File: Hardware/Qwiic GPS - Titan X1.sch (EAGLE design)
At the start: 33 parts, among them J1 U.FL, J2 SMD, J3 PTH, J4 SMD, U1 TITAN X1 GPS

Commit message: Added SparkX models to Sparkfun Library
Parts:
- B1: value COIN CELL -> 6.8MM_COIN_CELL; device SparkX:6.8MM_COIN_CELL -> SparkFun-Batteries:BATTERY-6.8MM_SMD
- J1: device SparkX:U.FL -> SparkFun-Connectors:U.FL2PIN
- J2, J4: value SMD -> Qwiic Right Angle; device SparkX:I2C_STANDARDJS-1MM -> SparkFun-Connectors:I2C_STANDARDQWIIC
- U1: value TITAN X1 GPS -> Titan X1 GPS; device SparkX:TITAN_X1_GPS -> SparkFun-GPS:TITAN_X1_GPS
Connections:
- net 3.3V: now also J2.2, J4.2; no longer J2.VCC, J4.VCC
- net GND: now also J2.1, J4.1; no longer J2.GND, J4.GND
- net SCL: now also J2.4, J4.4; no longer J2.SCL, J4.SCL
- net SDA: now also J2.3, J4.3; no longer J2.SDA, J4.SDA
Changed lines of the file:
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@@
 <part name="JP6" library="SparkFun" deviceset="FIDUCIAL" device="UFIDUCIAL"/>
 <part name="SUPPLY4" library="SparkFun-PowerSymbols" deviceset="3.3V" device=""/>
-<part name="J2" library="SparkX" deviceset="I2C_STANDARD" device="JS-1MM" value="SMD"/>
+<part name="J2" library="SparkFun-Connectors" deviceset="I2C_STANDARD" device="QWIIC" value="Qwiic Right Angle"/>
 <part name="GND6" library="SparkFun" deviceset="GND" device=""/>
 <part name="SUPPLY7" library="SparkFun-PowerSymbols" deviceset="3.3V" device=""/>
@@
 <part name="FRAME1" library="SparkFun-Aesthetics" deviceset="FRAME-LETTER" device=""/>
 <part name="SUPPLY8" library="SparkFun-PowerSymbols" deviceset="3.3V" device=""/>
-<part name="J4" library="SparkX" deviceset="I2C_STANDARD" device="JS-1MM" value="SMD"/>
+<part name="J4" library="SparkFun-Connectors" deviceset="I2C_STANDARD" device="QWIIC" value="Qwiic Right Angle"/>
 <part name="GND8" library="SparkFun" deviceset="GND" device=""/>
 <part name="LOGO1" library="SparkFun-Aesthetics" deviceset="OSHW-LOGO" device="MINI"/>
@@
 <part name="FB1" library="SparkFun-Coils" deviceset="FERRITE_BEAD" device="-0603" value="600Ohm/100MHz"/>
 <part name="C3" library="SparkFun-Capacitors" deviceset="1.0UF" device="-0603-16V-10%" value="1.0uF"/>
-<part name="B1" library="SparkX" deviceset="6.8MM_COIN_CELL" device="" value="COIN CELL"/>
+<part name="B1" library="SparkFun-Batteries" deviceset="BATTERY" device="-6.8MM_SMD" value="6.8MM_COIN_CELL"/>
 <part name="GND5" library="SparkFun-PowerSymbols" deviceset="GND" device=""/>
 <part name="GND9" library="SparkFun-PowerSymbols" deviceset="GND" device=""/>
 <part name="GND10" library="SparkFun-PowerSymbols" deviceset="GND" device=""/>
 <part name="GND11" library="SparkFun-PowerSymbols" deviceset="GND" device=""/>
-<part name="U1" library="SparkX" deviceset="TITAN_X1_GPS" device="" value="TITAN X1 GPS"/>
+<part name="U1" library="SparkFun-GPS" deviceset="TITAN_X1_GPS" device="" value="Titan X1 GPS"/>
 <part name="SUPPLY6" library="SparkFun-PowerSymbols" deviceset="3.3V" device=""/>
 <part name="R7" library="SparkFun-Resistors" deviceset="4.7KOHM" device="-0603-1/10W-1%" value="4.7k"/>
@@
 <part name="J7" library="SparkFun-Connectors" deviceset="CONN_05" device="NO_SILK"/>
 <part name="R11" library="SparkFun-Resistors" deviceset="470OHM" device="-0603-1/10W-1%" value="470"/>
-<part name="J1" library="SparkX" deviceset="U.FL" device="" value="U.FL"/>
+<part name="J1" library="SparkFun-Connectors" deviceset="U.FL2PIN" device="" value="U.FL"/>
 <part name="LOGO2" library="SparkFun-Aesthetics" deviceset="SFE_LOGO_NAME_FLAME" device=".1_INCH"/>
 </parts>
@@
 <instance part="JP6" gate="G$1" x="236.22" y="30.48"/>
 <instance part="SUPPLY4" gate="G$1" x="93.98" y="68.58"/>
-<instance part="J2" gate="G$1" x="104.14" y="60.96" rot="MR0"/>
+<instance part="J2" gate="G$1" x="104.14" y="60.96" smashed="yes" rot="MR0">
+<attribute name="VALUE" x="112.014" y="76.2" size="1.778" layer="96" font="vector" rot="MR270" align="top-left"/>
+<attribute name="NAME" x="109.22" y="68.834" size="1.778" layer="95" font="vector" rot="MR0"/>
+</instance>
 <instance part="GND6" gate="1" x="93.98" y="53.34"/>
 <instance part="SUPPLY7" gate="G$1" x="127" y="68.58"/>
@@
 <instance part="FRAME1" gate="V" x="147.32" y="0"/>
 <instance part="SUPPLY8" gate="G$1" x="93.98" y="40.64"/>
-<instance part="J4" gate="G$1" x="104.14" y="33.02" rot="MR0"/>
+<instance part="J4" gate="G$1" x="104.14" y="33.02" smashed="yes" rot="MR0">
+<attribute name="VALUE" x="112.014" y="48.26" size="1.778" layer="96" font="vector" rot="MR270" align="top-left"/>
+<attribute name="NAME" x="109.22" y="40.894" size="1.778" layer="95" font="vector" rot="MR0"/>
+</instance>
 <instance part="GND8" gate="1" x="93.98" y="25.4"/>
 <instance part="LOGO1" gate="G$1" x="233.68" y="48.26"/>
@@
 <net name="3.3V" class="0">
 <segment>
-<pinref part="J2" gate="G$1" pin="VCC"/>
+<pinref part="J2" gate="G$1" pin="2"/>
 <wire x1="96.52" y1="60.96" x2="93.98" y2="60.96" width="0.1524" layer="91"/>
 <wire x1="93.98" y1="60.96" x2="93.98" y2="68.58" width="0.1524" layer="91"/>
@@
 </segment>
 <segment>
-<pinref part="J4" gate="G$1" pin="VCC"/>
+<pinref part="J4" gate="G$1" pin="2"/>
 <wire x1="96.52" y1="33.02" x2="93.98" y2="33.02" width="0.1524" layer="91"/>
 <wire x1="93.98" y1="33.02" x2="93.98" y2="40.64" width="0.1524" layer="91"/>
@@
 <net name="GND" class="0">
 <segment>
-<pinref part="J2" gate="G$1" pin="GND"/>
+<pinref part="J2" gate="G$1" pin="1"/>
 <wire x1="96.52" y1="58.42" x2="93.98" y2="58.42" width="0.1524" layer="91"/>
 <wire x1="93.98" y1="58.42" x2="93.98" y2="55.88" width="0.1524" layer="91"/>
@@
 </segment>
 <segment>
-<pinref part="J4" gate="G$1" pin="GND"/>
+<pinref part="J4" gate="G$1" pin="1"/>
 <wire x1="96.52" y1="30.48" x2="93.98" y2="30.48" width="0.1524" layer="91"/>
 <wire x1="93.98" y1="30.48" x2="93.98" y2="27.94" width="0.1524" layer="91"/>
@@
 <net name="SCL" class="0">
 <segment>
-<pinref part="J2" gate="G$1" pin="SCL"/>
+<pinref part="J2" gate="G$1" pin="4"/>
 <wire x1="96.52" y1="66.04" x2="91.44" y2="66.04" width="0.1524" layer="91"/>
 <label x="91.44" y="66.04" size="1.27" layer="95" rot="R180" xref="yes"/>
@@
 </segment>
 <segment>
-<pinref part="J4" gate="G$1" pin="SCL"/>
+<pinref part="J4" gate="G$1" pin="4"/>
 <wire x1="96.52" y1="38.1" x2="91.44" y2="38.1" width="0.1524" layer="91"/>
 <label x="91.44" y="38.1" size="1.27" layer="95" rot="R180" xref="yes"/>
@@
 <net name="SDA" class="0">
 <segment>
-<pinref part="J2" gate="G$1" pin="SDA"/>
+<pinref part="J2" gate="G$1" pin="3"/>
 <wire x1="96.52" y1="63.5" x2="91.44" y2="63.5" width="0.1524" layer="91"/>
 <label x="91.44" y="63.5" size="1.27" layer="95" rot="R180" xref="yes"/>
@@
 </segment>
 <segment>
-<pinref part="J4" gate="G$1" pin="SDA"/>
+<pinref part="J4" gate="G$1" pin="3"/>
 <wire x1="96.52" y1="35.56" x2="91.44" y2="35.56" width="0.1524" layer="91"/>
 <label x="91.44" y="35.56" size="1.27" layer="95" rot="R180" xref="yes"/>

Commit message: fixed DRC errors, updated board to meet checklist
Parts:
- added JP7, JP8: FIDUCIALUFIDUCIAL, SparkFun:FIDUCIALUFIDUCIAL
- added LOGO3: REVISION, SparkFun-Aesthetics:REVISION
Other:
- note added: "Andrew England"
- note added: "V01"
- note removed: "X10"
- moved on the sheet: D1, JP5, R11
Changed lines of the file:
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@@
 <part name="J1" library="SparkFun-Connectors" deviceset="U.FL2PIN" device="" value="U.FL"/>
 <part name="LOGO2" library="SparkFun-Aesthetics" deviceset="SFE_LOGO_NAME_FLAME" device=".1_INCH"/>
+<part name="LOGO3" library="SparkFun-Aesthetics" deviceset="REVISION" device=""/>
+<part name="JP7" library="SparkFun" deviceset="FIDUCIAL" device="UFIDUCIAL"/>
+<part name="JP8" library="SparkFun" deviceset="FIDUCIAL" device="UFIDUCIAL"/>
 </parts>
 <sheets>
@@
 <plain>
 <text x="170.434" y="11.43" size="2.54" layer="94">N. Seidle</text>
-<text x="237.744" y="7.366" size="2.54" layer="94">X10</text>
+<text x="237.744" y="7.366" size="2.54" layer="94">V01</text>
 <text x="152.4" y="88.9" size="1.778" layer="97" align="center">7-bit unshifted I2C address: 0x10</text>
 <text x="153.162" y="165.862" size="2.54" layer="94" ratio="15" rot="MR180" align="center">Titan X1 GPS</text>
 <text x="31.242" y="165.862" size="2.54" layer="94" ratio="15" rot="MR180" align="center">RTC Backup</text>
-<text x="31.242" y="87.122" size="2.54" layer="94" ratio="15" rot="MR180" align="center">Pulse Per Second LED</text>
+<text x="31.242" y="71.882" size="2.54" layer="94" ratio="15" rot="MR180" align="center">Pulse Per Second LED</text>
 <text x="93.98" y="119.38" size="1.778" layer="97">50 Ohm
 Microstrip: 0.0585"
 PCB: 0.8mm
 </text>
+<text x="174.752" y="7.112" size="2.54" layer="94">Andrew England</text>
+<wire x1="0" y1="81.28" x2="248.92" y2="81.28" width="0.1524" layer="97" style="longdash"/>
+<wire x1="63.5" y1="185.42" x2="63.5" y2="0" width="0.1524" layer="97" style="longdash"/>
 </plain>
 <instances>
 <instance part="JP3" gate="G$1" x="246.38" y="30.48"/>
 <instance part="JP4" gate="G$1" x="246.38" y="27.94"/>
-<instance part="JP2" gate="G$1" x="231.14" y="30.48"/>
+<instance part="JP2" gate="G$1" x="233.68" y="30.48" rot="R270"/>
 <instance part="JP6" gate="G$1" x="236.22" y="30.48"/>
 <instance part="SUPPLY4" gate="G$1" x="93.98" y="68.58"/>
@@
 </instance>
 <instance part="SUPPLY9" gate="G$1" x="208.28" y="154.94"/>
-<instance part="GND4" gate="1" x="22.86" y="33.02"/>
-<instance part="D1" gate="G$1" x="22.86" y="43.18"/>
+<instance part="GND4" gate="1" x="22.86" y="25.4"/>
+<instance part="D1" gate="G$1" x="22.86" y="35.56"/>
 <instance part="GND12" gate="1" x="88.9" y="121.92"/>
-<instance part="JP5" gate="G$1" x="22.86" y="66.04" rot="R90"/>
+<instance part="JP5" gate="G$1" x="22.86" y="55.88" rot="R90"/>
 <instance part="L1" gate="G$1" x="96.52" y="139.7" smashed="yes" rot="R180">
 <attribute name="NAME" x="91.948" y="141.732" size="1.778" layer="95" font="vector"/>
@@
 <instance part="R5" gate="G$1" x="22.86" y="137.16" rot="R90"/>
 <instance part="J7" gate="G$1" x="137.16" y="30.48" rot="R180"/>
-<instance part="R11" gate="G$1" x="22.86" y="53.34" smashed="yes" rot="R90">
-<attribute name="NAME" x="26.162" y="50.292" size="1.778" layer="95" font="vector" rot="R90" align="bottom-center"/>
-<attribute name="VALUE" x="26.162" y="55.118" size="1.778" layer="96" font="vector" rot="R270" align="top-center"/>
+<instance part="R11" gate="G$1" x="22.86" y="45.72" smashed="yes" rot="R90">
+<attribute name="NAME" x="26.162" y="42.672" size="1.778" layer="95" font="vector" rot="R90" align="bottom-center"/>
+<attribute name="VALUE" x="26.162" y="47.498" size="1.778" layer="96" font="vector" rot="R270" align="top-center"/>
 </instance>
 <instance part="J1" gate="G$1" x="88.9" y="132.08" smashed="yes">
@@
 </instance>
 <instance part="LOGO2" gate="G$1" x="162.56" y="35.56"/>
+<instance part="LOGO3" gate="G$1" x="148.59" y="7.112"/>
+<instance part="JP7" gate="G$1" x="233.68" y="27.94" rot="R270"/>
+<instance part="JP8" gate="G$1" x="236.22" y="27.94" rot="R270"/>
 </instances>
 <busses>
@@
 <segment>
 <pinref part="D1" gate="G$1" pin="C"/>
-<wire x1="22.86" y1="38.1" x2="22.86" y2="35.56" width="0.1524" layer="91"/>
+<wire x1="22.86" y1="30.48" x2="22.86" y2="27.94" width="0.1524" layer="91"/>
 <pinref part="GND4" gate="1" pin="GND"/>
 </segment>
@@
 </segment>
 <segment>
-<wire x1="22.86" y1="73.66" x2="25.4" y2="73.66" width="0.1524" layer="91"/>
-<label x="25.4" y="73.66" size="1.27" layer="95" xref="yes"/>
+<wire x1="22.86" y1="60.96" x2="25.4" y2="60.96" width="0.1524" layer="91"/>
+<label x="25.4" y="60.96" size="1.27" layer="95" xref="yes"/>
 <pinref part="JP5" gate="G$1" pin="2"/>
-<wire x1="22.86" y1="71.12" x2="22.86" y2="73.66" width="0.1524" layer="91"/>
 </segment>
 </net>
@@
 <segment>
 <pinref part="D1" gate="G$1" pin="A"/>
-<wire x1="22.86" y1="48.26" x2="22.86" y2="45.72" width="0.1524" layer="91"/>
+<wire x1="22.86" y1="40.64" x2="22.86" y2="38.1" width="0.1524" layer="91"/>
 <pinref part="R11" gate="G$1" pin="1"/>
 </segment>
@@
 <segment>
 <pinref part="JP5" gate="G$1" pin="1"/>
-<wire x1="22.86" y1="60.96" x2="22.86" y2="58.42" width="0.1524" layer="91"/>
 <pinref part="R11" gate="G$1" pin="2"/>
 </segment>

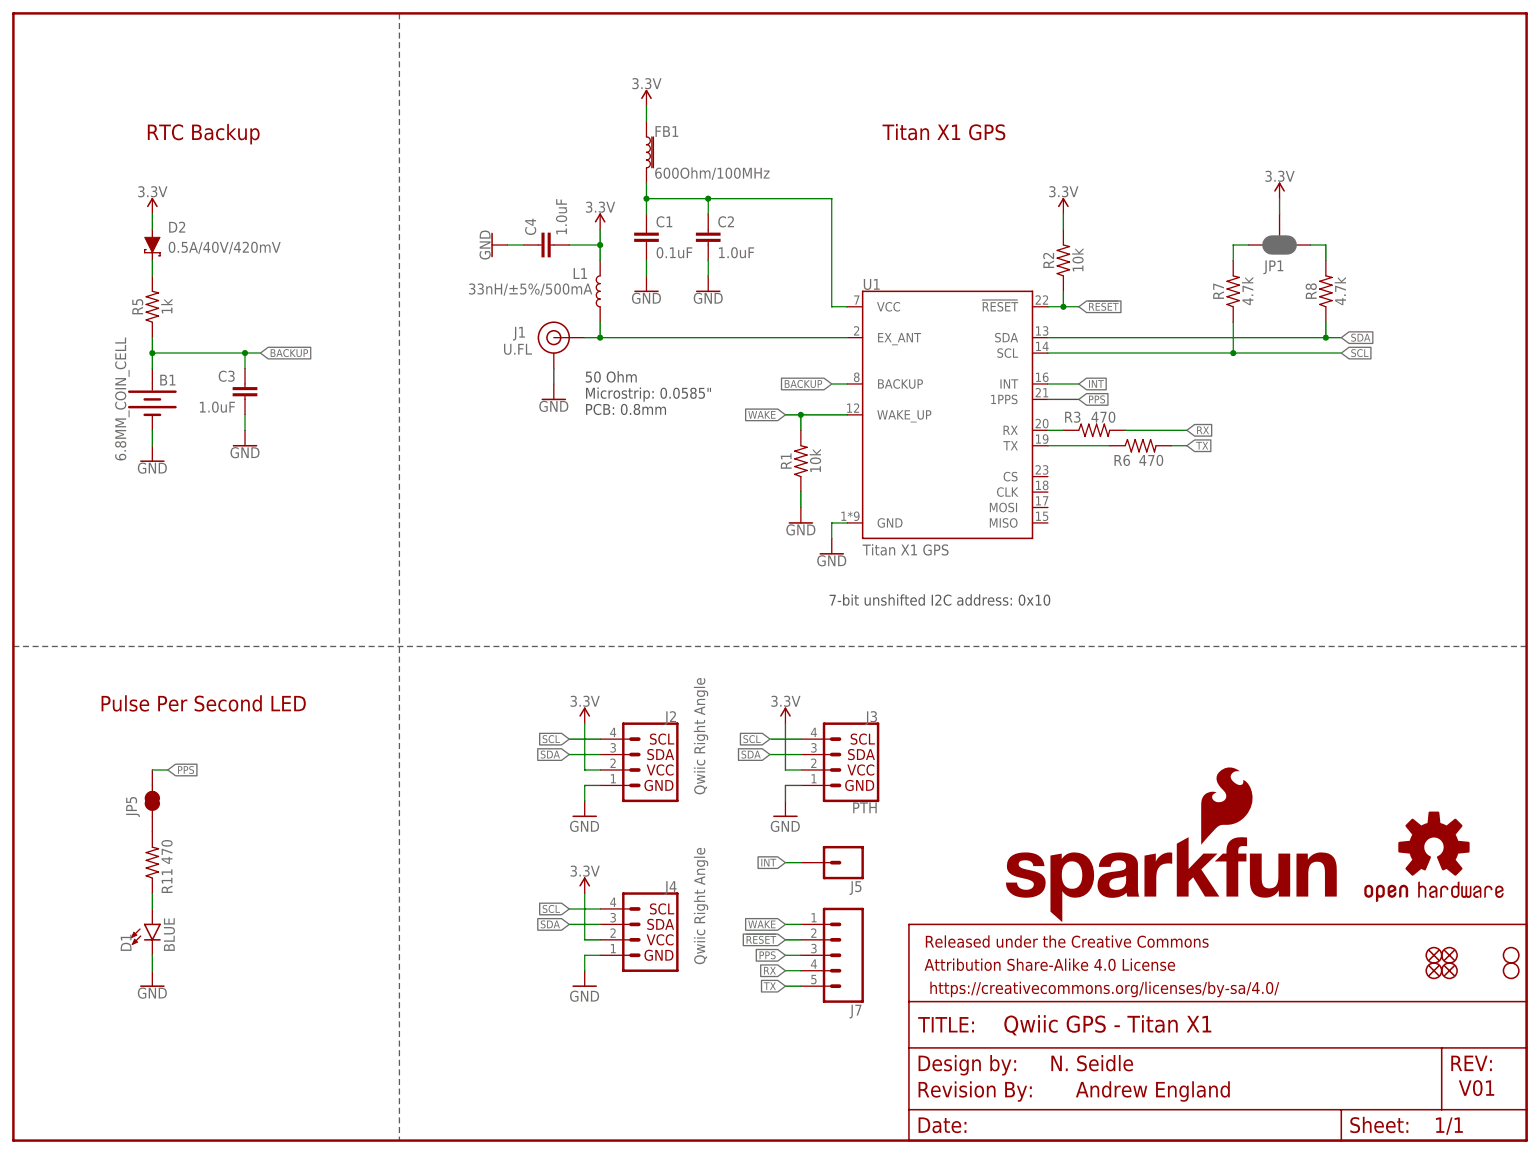
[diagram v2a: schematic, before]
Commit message: Added jumper functions to schematic and board
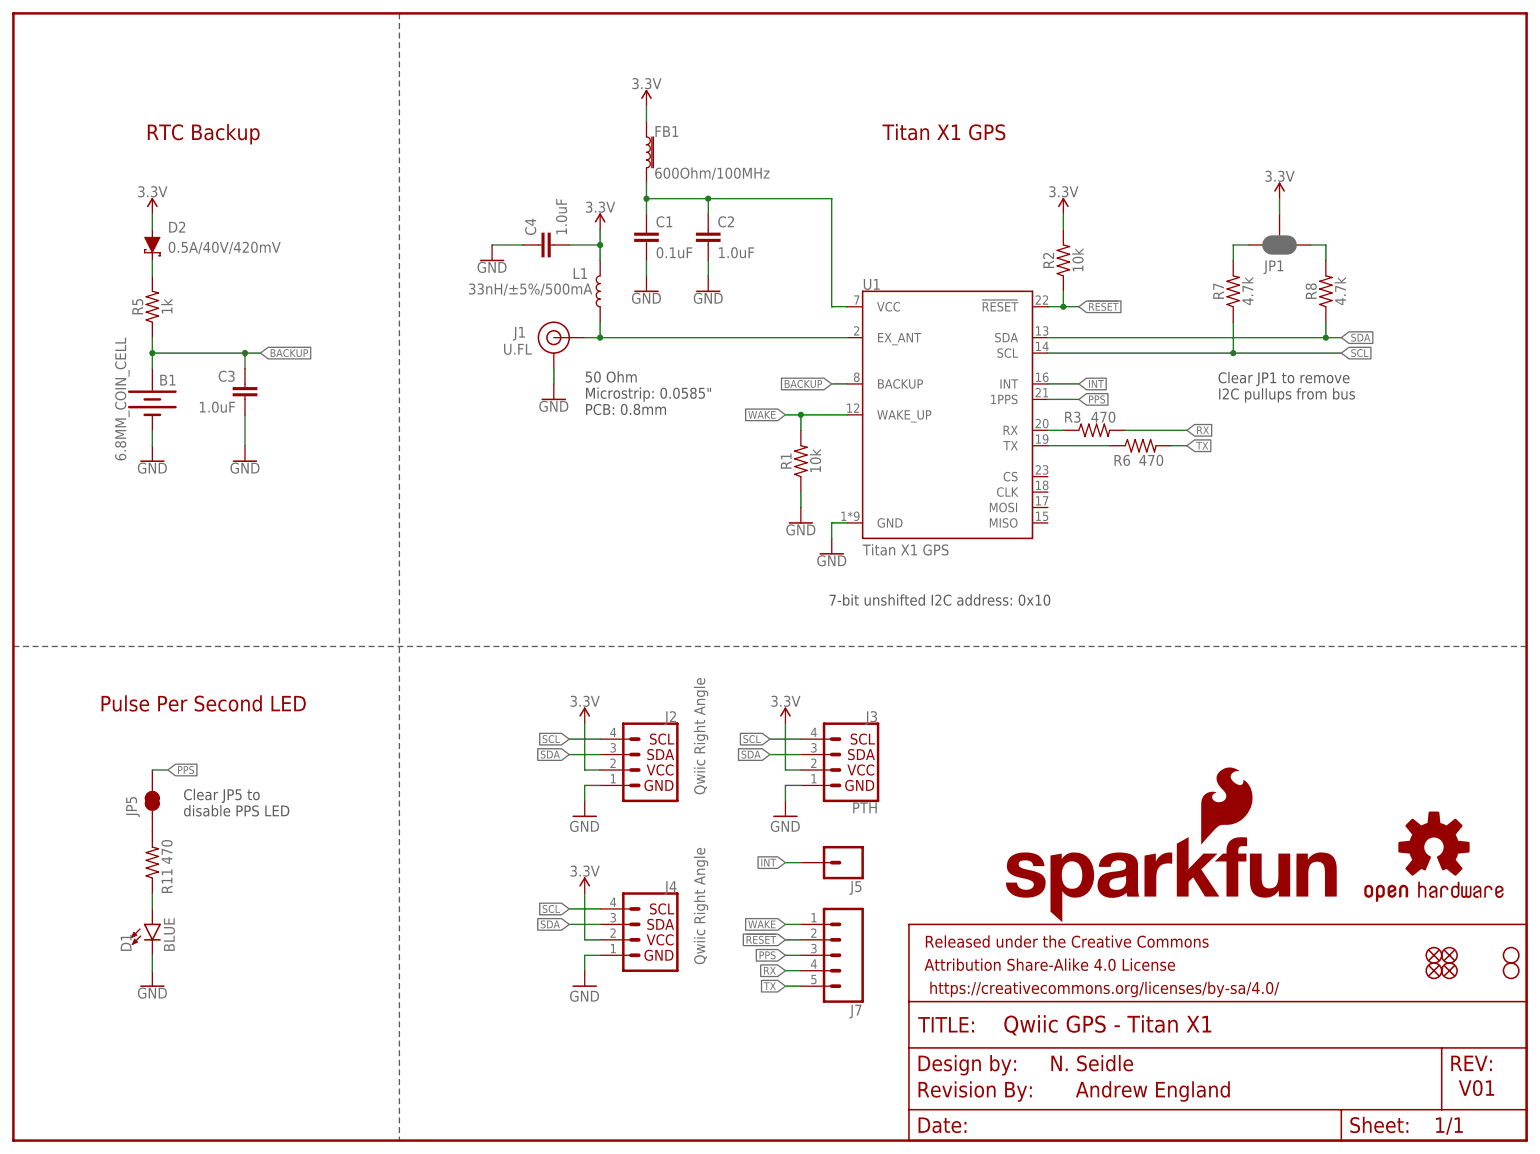
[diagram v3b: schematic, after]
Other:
- note added: "Clear JP1 to remove I2C pullups from bus"
- note added: "Clear JP5 to disable PPS LED"
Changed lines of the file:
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@@
 <wire x1="0" y1="81.28" x2="248.92" y2="81.28" width="0.1524" layer="97" style="longdash"/>
 <wire x1="63.5" y1="185.42" x2="63.5" y2="0" width="0.1524" layer="97" style="longdash"/>
+<text x="198.12" y="121.92" size="1.778" layer="97">Clear JP1 to remove
+I2C pullups from bus</text>
+<text x="27.94" y="53.34" size="1.778" layer="97">Clear JP5 to
+disable PPS LED</text>
 </plain>
 <instances>
@@
 <instance part="GND5" gate="1" x="22.86" y="111.76"/>
 <instance part="GND9" gate="1" x="129.54" y="101.6"/>
-<instance part="GND10" gate="1" x="38.1" y="114.3"/>
+<instance part="GND10" gate="1" x="38.1" y="111.76"/>
 <instance part="GND11" gate="1" x="104.14" y="139.7" rot="MR0"/>
 <instance part="U1" gate="U1" x="154.94" y="119.38"/>
@@
 </instance>
 <instance part="C4" gate="G$1" x="88.9" y="147.32" rot="R90"/>
-<instance part="GND13" gate="1" x="78.74" y="147.32" rot="R270"/>
+<instance part="GND13" gate="1" x="78.74" y="144.78"/>
 <instance part="SUPPLY3" gate="G$1" x="96.52" y="149.86" rot="MR0"/>
 <instance part="D2" gate="G$1" x="22.86" y="147.32" smashed="yes" rot="R270">
@@
 <segment>
 <pinref part="C3" gate="G$1" pin="2"/>
-<wire x1="38.1" y1="119.38" x2="38.1" y2="116.84" width="0.1524" layer="91"/>
+<wire x1="38.1" y1="119.38" x2="38.1" y2="114.3" width="0.1524" layer="91"/>
 <pinref part="GND10" gate="1" pin="GND"/>
 </segment>
@@
 <pinref part="C4" gate="G$1" pin="1"/>
 <pinref part="GND13" gate="1" pin="GND"/>
-<wire x1="81.28" y1="147.32" x2="83.82" y2="147.32" width="0.1524" layer="91"/>
-</segment>
-<segment>
+<wire x1="78.74" y1="147.32" x2="83.82" y2="147.32" width="0.1524" layer="91"/>
+</segment>
+<segment>
